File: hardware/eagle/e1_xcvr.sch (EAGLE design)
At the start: 48 parts, among them T1 BC847C

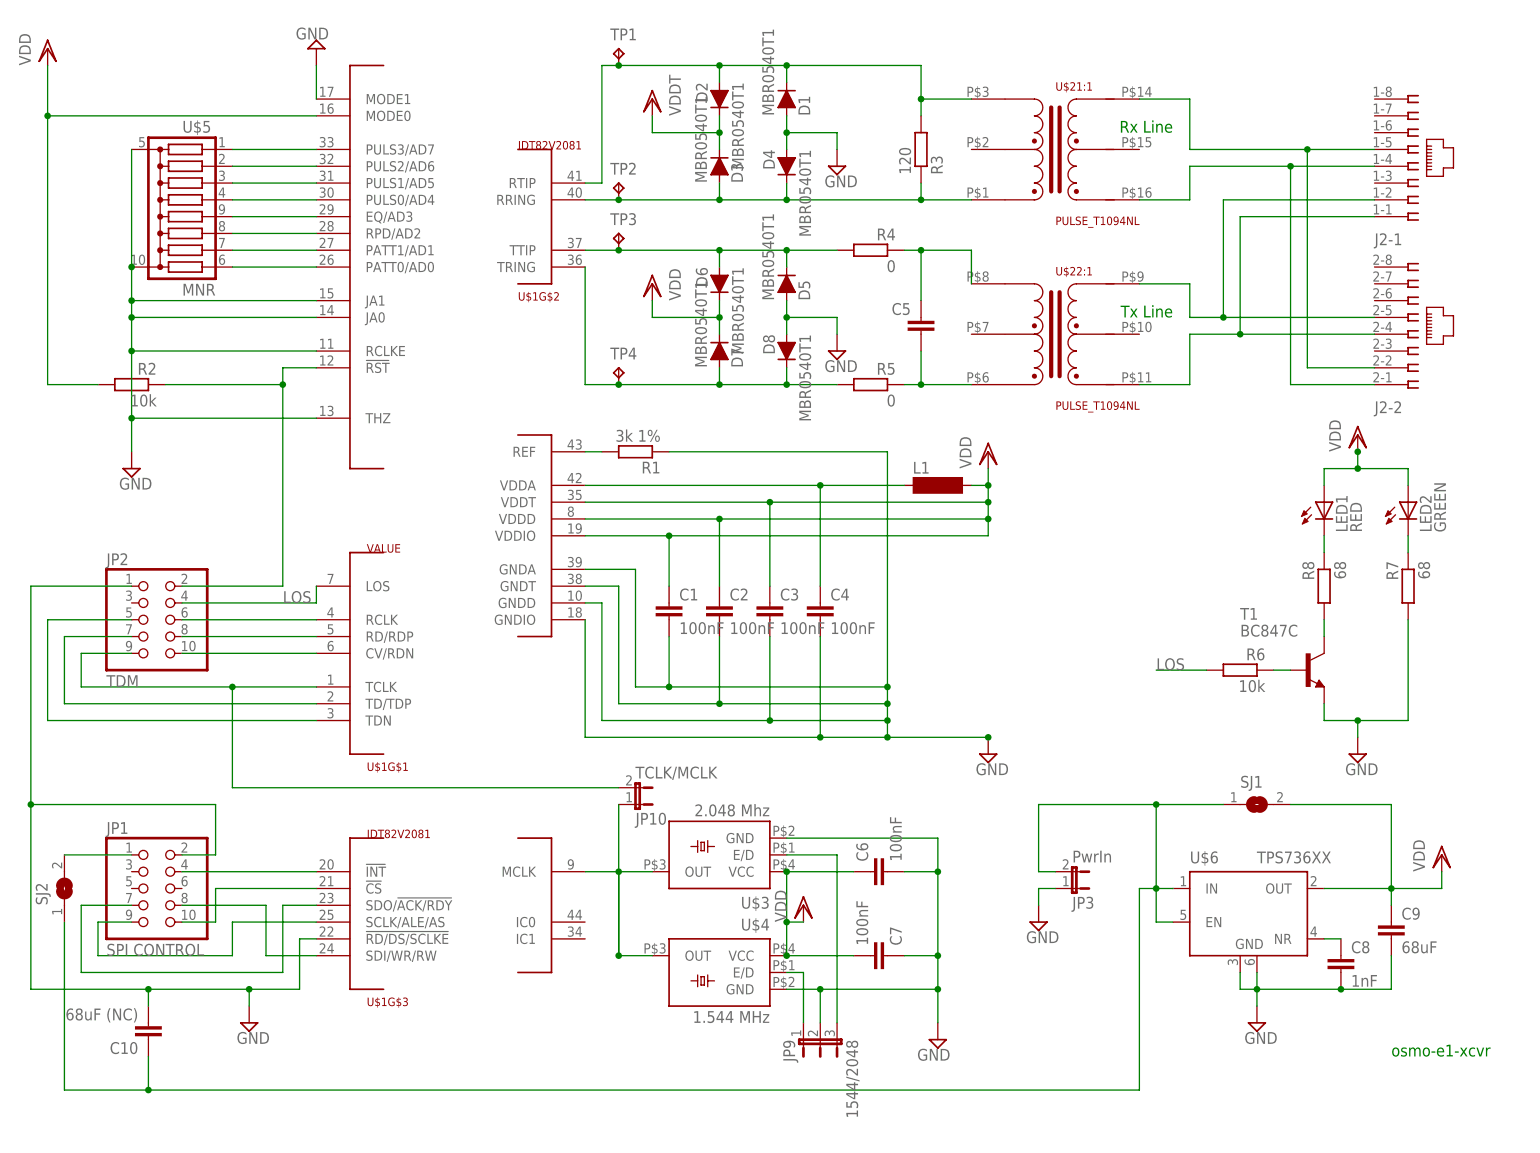
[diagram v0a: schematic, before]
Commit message: give parts names without "$", use 47nH as L1 (1206)
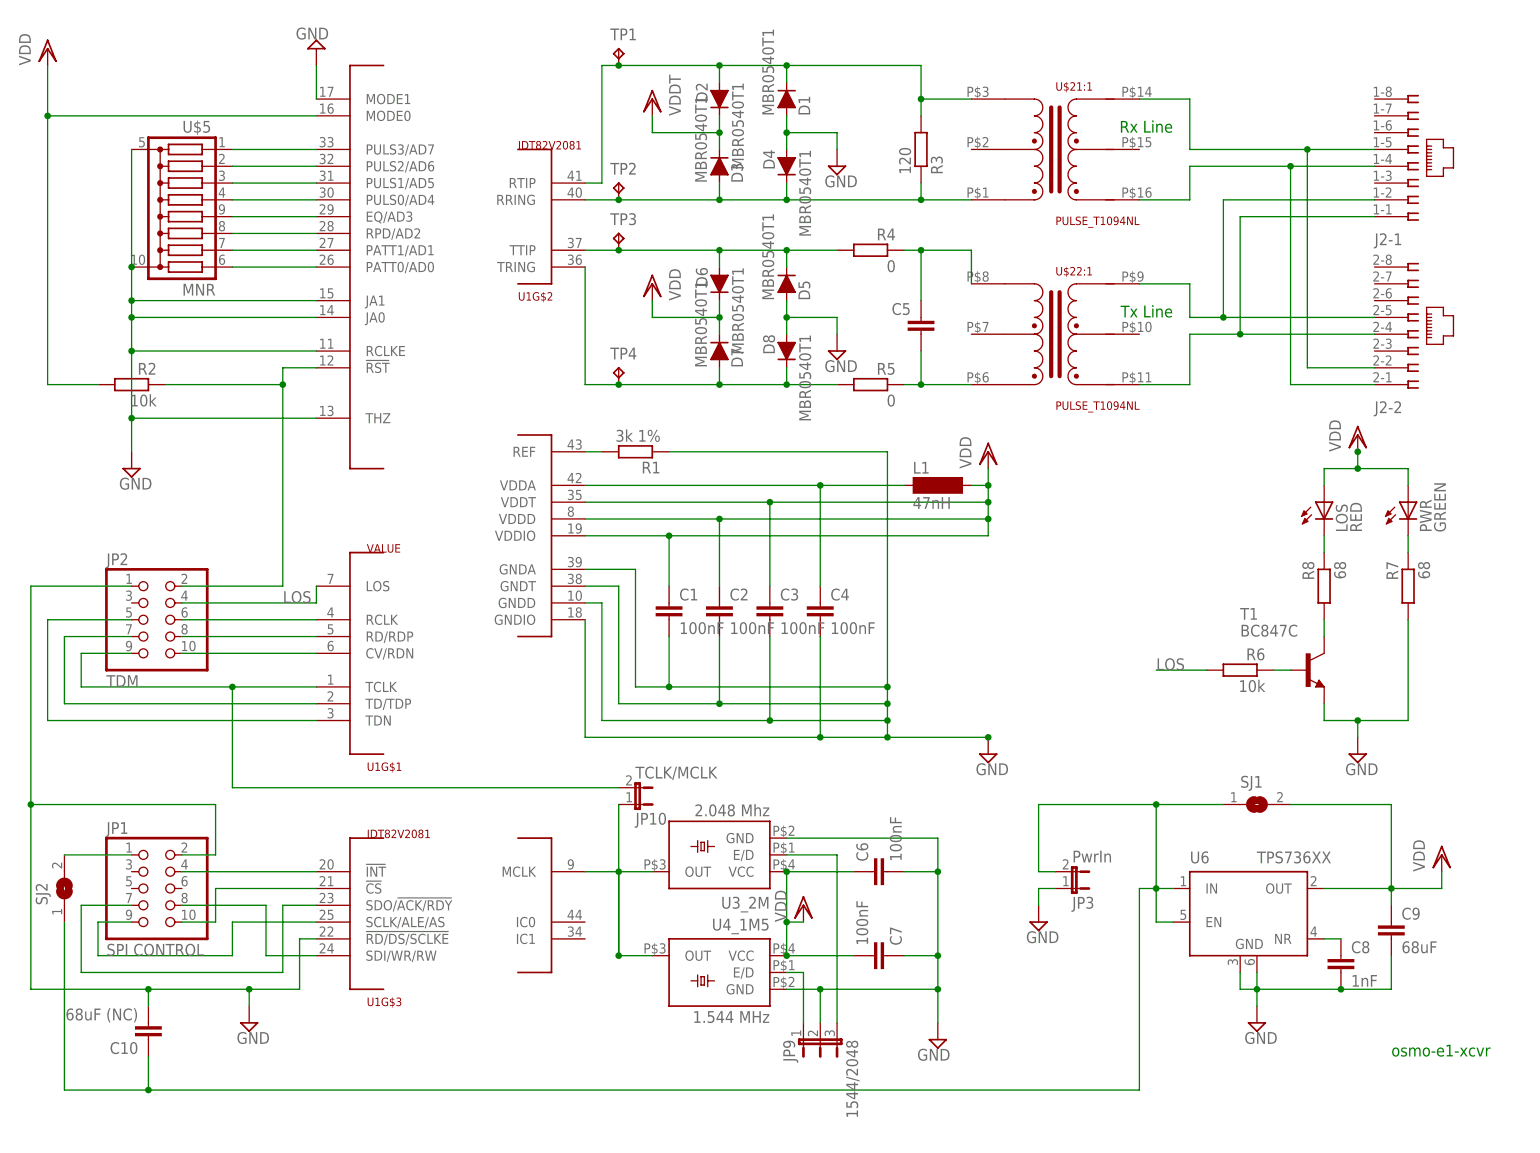
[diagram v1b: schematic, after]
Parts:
- L1: value (none) -> 47nH
- renumbered LED1 to LOS, LED2 to PWR, U$1 to U1, U$3 to U3_2M, U$4 to U4_1M5, U$6 to U6

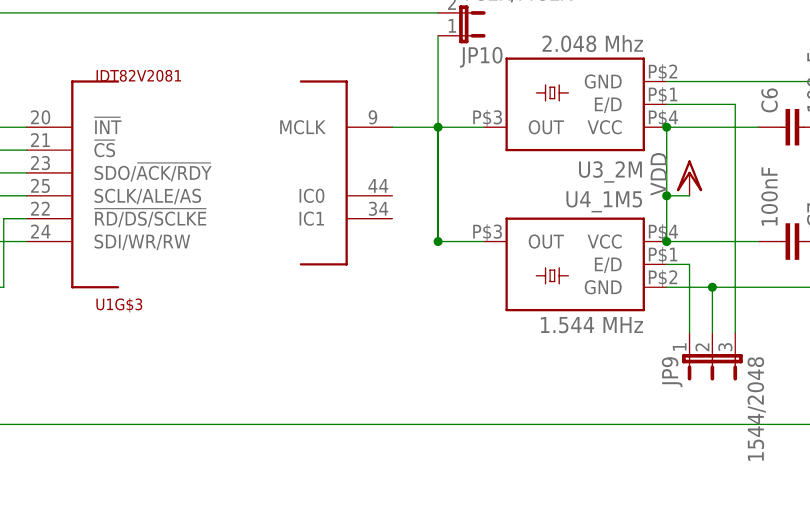
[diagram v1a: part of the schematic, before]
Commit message: connect LIU's pin 44 to GND (solves OSM#3247)
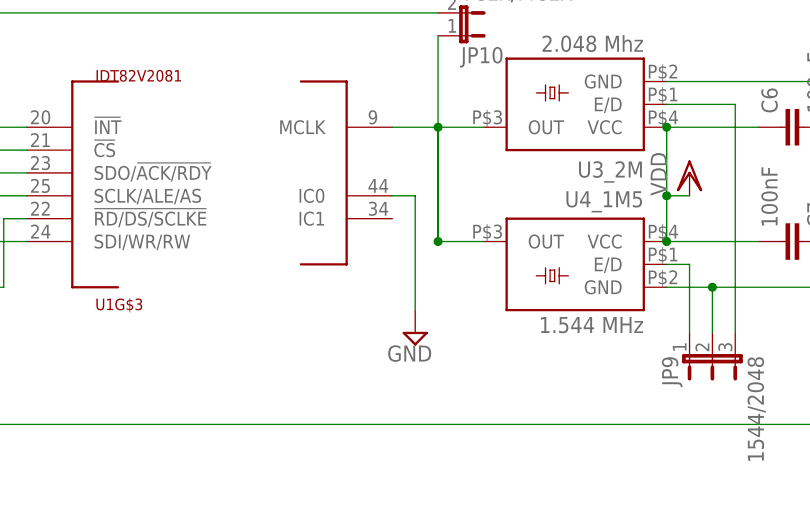
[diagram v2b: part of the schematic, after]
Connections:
- net GND: now also U1G$6.IC0
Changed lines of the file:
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@@
 <?xml version="1.0" encoding="utf-8"?>
 <!DOCTYPE eagle SYSTEM "eagle.dtd">
-<eagle version="6.0">
+<eagle version="7.6.0">
 <drawing>
 <settings>
@@
 <grid distance="0.1" unitdist="inch" unit="inch" style="lines" multiple="1" display="no" altdistance="0.01" altunitdist="inch" altunit="inch"/>
 <layers>
-<layer number="1" name="Top" color="4" fill="1" visible="no" active="no"/>
-<layer number="16" name="Bottom" color="1" fill="1" visible="no" active="no"/>
-<layer number="17" name="Pads" color="2" fill="1" visible="no" active="no"/>
-<layer number="18" name="Vias" color="2" fill="1" visible="no" active="no"/>
-<layer number="19" name="Unrouted" color="6" fill="1" visible="no" active="no"/>
-<layer number="20" name="Dimension" color="15" fill="1" visible="no" active="no"/>
-<layer number="21" name="tPlace" color="7" fill="1" visible="no" active="no"/>
-<layer number="22" name="bPlace" color="7" fill="1" visible="no" active="no"/>
-<layer number="23" name="tOrigins" color="15" fill="1" visible="no" active="no"/>
-<layer number="24" name="bOrigins" color="15" fill="1" visible="no" active="no"/>
-<layer number="25" name="tNames" color="7" fill="1" visible="no" active="no"/>
-<layer number="26" name="bNames" color="7" fill="1" visible="no" active="no"/>
-<layer number="27" name="tValues" color="7" fill="1" visible="no" active="no"/>
-<layer number="28" name="bValues" color="7" fill="1" visible="no" active="no"/>
+<layer number="1" name="Top" color="4" fill="1" visible="yes" active="no"/>
+<layer number="16" name="Bottom" color="1" fill="1" visible="yes" active="no"/>
+<layer number="17" name="Pads" color="2" fill="1" visible="yes" active="no"/>
+<layer number="18" name="Vias" color="2" fill="1" visible="yes" active="no"/>
+<layer number="19" name="Unrouted" color="6" fill="1" visible="yes" active="no"/>
+<layer number="20" name="Dimension" color="15" fill="1" visible="yes" active="no"/>
+<layer number="21" name="tPlace" color="7" fill="1" visible="yes" active="no"/>
+<layer number="22" name="bPlace" color="7" fill="1" visible="yes" active="no"/>
+<layer number="23" name="tOrigins" color="15" fill="1" visible="yes" active="no"/>
+<layer number="24" name="bOrigins" color="15" fill="1" visible="yes" active="no"/>
+<layer number="25" name="tNames" color="7" fill="1" visible="yes" active="no"/>
+<layer number="26" name="bNames" color="7" fill="1" visible="yes" active="no"/>
+<layer number="27" name="tValues" color="7" fill="1" visible="yes" active="no"/>
+<layer number="28" name="bValues" color="7" fill="1" visible="yes" active="no"/>
 <layer number="29" name="tStop" color="7" fill="3" visible="no" active="no"/>
 <layer number="30" name="bStop" color="7" fill="6" visible="no" active="no"/>
@@
 <layer number="35" name="tGlue" color="7" fill="4" visible="no" active="no"/>
 <layer number="36" name="bGlue" color="7" fill="5" visible="no" active="no"/>
-<layer number="37" name="tTest" color="7" fill="1" visible="no" active="no"/>
-<layer number="38" name="bTest" color="7" fill="1" visible="no" active="no"/>
+<layer number="37" name="tTest" color="7" fill="1" visible="yes" active="no"/>
+<layer number="38" name="bTest" color="7" fill="1" visible="yes" active="no"/>
 <layer number="39" name="tKeepout" color="4" fill="11" visible="no" active="no"/>
 <layer number="40" name="bKeepout" color="1" fill="11" visible="no" active="no"/>
@@
 <layer number="44" name="Drills" color="7" fill="1" visible="no" active="no"/>
 <layer number="45" name="Holes" color="7" fill="1" visible="no" active="no"/>
-<layer number="46" name="Milling" color="3" fill="1" visible="no" active="no"/>
-<layer number="47" name="Measures" color="7" fill="1" visible="no" active="no"/>
-<layer number="48" name="Document" color="7" fill="1" visible="no" active="no"/>
-<layer number="49" name="Reference" color="7" fill="1" visible="no" active="no"/>
-<layer number="51" name="tDocu" color="7" fill="1" visible="no" active="no"/>
-<layer number="52" name="bDocu" color="7" fill="1" visible="no" active="no"/>
+<layer number="46" name="Milling" color="3" fill="1" visible="yes" active="no"/>
+<layer number="47" name="Measures" color="7" fill="1" visible="yes" active="no"/>
+<layer number="48" name="Document" color="7" fill="1" visible="yes" active="no"/>
+<layer number="49" name="Reference" color="7" fill="1" visible="yes" active="no"/>
+<layer number="51" name="tDocu" color="7" fill="1" visible="yes" active="no"/>
+<layer number="52" name="bDocu" color="7" fill="1" visible="yes" active="no"/>
 <layer number="91" name="Nets" color="2" fill="1" visible="yes" active="yes"/>
 <layer number="92" name="Busses" color="1" fill="1" visible="yes" active="yes"/>
@@
 <part name="SUPPLY9" library="supply2" deviceset="GND" device=""/>
 <part name="SUPPLY10" library="supply2" deviceset="GND" device=""/>
+<part name="SUPPLY11" library="supply2" deviceset="GND" device=""/>
 </parts>
 <sheets>
@@
 <instance part="SUPPLY9" gate="GND" x="10.16" y="144.78"/>
 <instance part="SUPPLY10" gate="GND" x="27.94" y="60.96"/>
+<instance part="SUPPLY11" gate="GND" x="81.28" y="60.96" rot="MR0"/>
 </instances>
 <busses>
@@
 <pinref part="SUPPLY9" gate="GND" pin="GND"/>
 </segment>
+<segment>
+<pinref part="U1" gate="G$6" pin="IC0"/>
+<pinref part="SUPPLY11" gate="GND" pin="GND"/>
+<wire x1="78.74" y1="76.2" x2="81.28" y2="76.2" width="0.1524" layer="91"/>
+<wire x1="81.28" y1="76.2" x2="81.28" y2="63.5" width="0.1524" layer="91"/>
+</segment>
 </net>

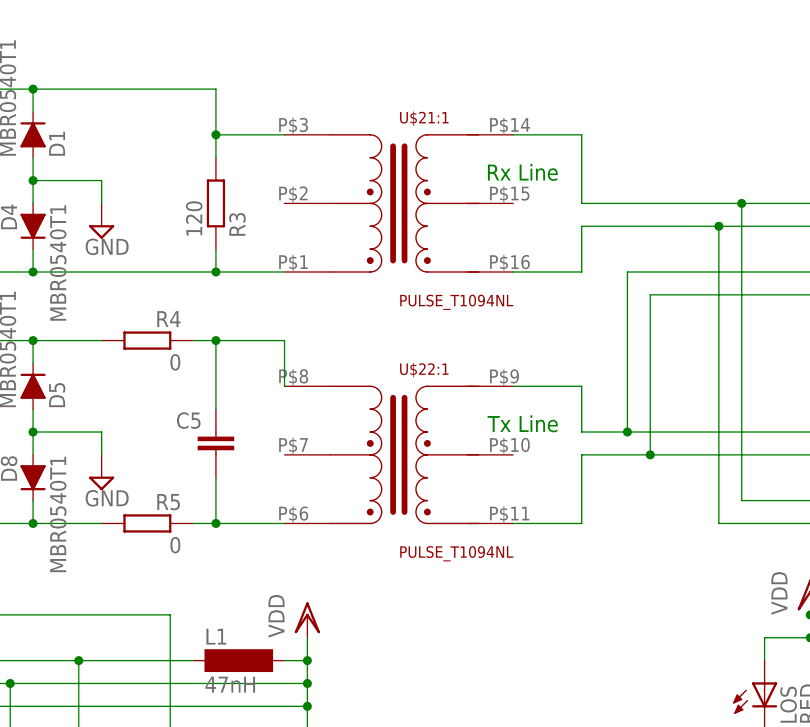
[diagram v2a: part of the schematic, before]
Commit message: replace old PULSE_T1094NL footprint, repair pin assignment (solves OSM#3269)
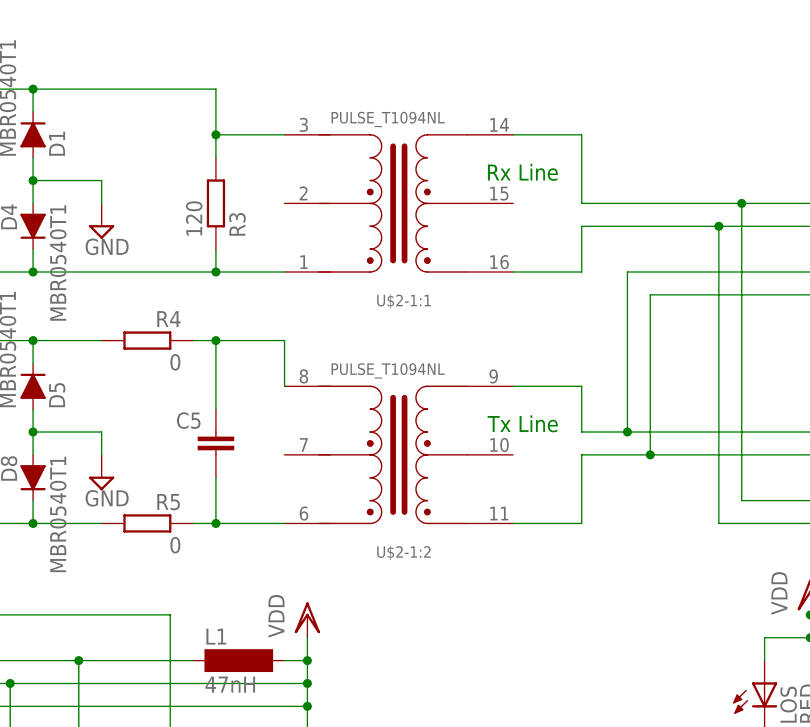
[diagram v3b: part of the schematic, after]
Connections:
- net N$29: now also U$2-1:2.P$6; no longer U$22:1.P$3
- net N$31: now also U$2-1:2.P$4; no longer U$22:1.P$1
- net N$32: now also U$2-1:2.P$3; no longer U$22:1.P$6
- net N$34: now also U$2-1:1.P$1; no longer U$21:1.P$4
- net N$36: now also U$2-1:2.P$1; no longer U$22:1.P$4
- net N$40: now also U$2-1:1.P$3; no longer U$21:1.P$6
- net RRING: now also U$2-1:1.P$4; no longer U$21:1.P$1
- net RTIP: now also U$2-1:1.P$6; no longer U$21:1.P$3
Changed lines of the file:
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@@
 <layers>
 <layer number="1" name="Top" color="4" fill="1" visible="yes" active="no"/>
+<layer number="2" name="Route2" color="1" fill="3" visible="yes" active="no"/>
+<layer number="3" name="Route3" color="4" fill="3" visible="yes" active="no"/>
+<layer number="14" name="Route14" color="1" fill="6" visible="yes" active="no"/>
+<layer number="15" name="Route15" color="4" fill="6" visible="yes" active="no"/>
 <layer number="16" name="Bottom" color="1" fill="1" visible="yes" active="no"/>
 <layer number="17" name="Pads" color="2" fill="1" visible="yes" active="no"/>
@@
 <instance part="C3" gate="G$1" x="106.68" y="124.46"/>
 <instance part="C4" gate="G$1" x="114.3" y="124.46"/>
-<instance part="U$2" gate="1:1" x="149.86" y="193.04" rot="MR180"/>
-<instance part="U$2" gate="2:1" x="149.86" y="165.1" rot="MR180"/>
+<instance part="U$2" gate="-1:1" x="149.86" y="193.04" rot="MR180"/>
+<instance part="U$2" gate="-1:2" x="149.86" y="165.1" rot="MR180"/>
 <instance part="R3" gate="G$1" x="129.54" y="193.04" rot="MR90"/>
 <instance part="D1" gate="G$1" x="109.22" y="200.66" rot="MR90"/>
@@
 <net name="RTIP" class="0">
 <segment>
-<pinref part="U$2" gate="1:1" pin="P$3"/>
+<pinref part="U$2" gate="-1:1" pin="P$6"/>
 <wire x1="137.16" y1="200.66" x2="129.54" y2="200.66" width="0.1524" layer="91"/>
 <pinref part="R3" gate="G$1" pin="2"/>
@@
 <net name="RRING" class="0">
 <segment>
-<pinref part="U$2" gate="1:1" pin="P$1"/>
+<pinref part="U$2" gate="-1:1" pin="P$4"/>
 <wire x1="137.16" y1="185.42" x2="129.54" y2="185.42" width="0.1524" layer="91"/>
 <pinref part="R3" gate="G$1" pin="1"/>
@@
 <net name="N$29" class="0">
 <segment>
-<pinref part="U$2" gate="2:1" pin="P$3"/>
+<pinref part="U$2" gate="-1:2" pin="P$6"/>
 <wire x1="137.16" y1="177.8" x2="137.16" y2="172.72" width="0.1524" layer="91"/>
 <pinref part="R4" gate="G$1" pin="1"/>
@@
 <segment>
 <pinref part="R5" gate="G$1" pin="1"/>
-<pinref part="U$2" gate="2:1" pin="P$1"/>
+<pinref part="U$2" gate="-1:2" pin="P$4"/>
 <wire x1="127" y1="157.48" x2="129.54" y2="157.48" width="0.1524" layer="91"/>
 <pinref part="C5" gate="G$1" pin="2"/>
@@
 <segment>
 <wire x1="170.18" y1="200.66" x2="162.56" y2="200.66" width="0.1524" layer="91"/>
-<pinref part="U$2" gate="1:1" pin="P$6"/>
+<pinref part="U$2" gate="-1:1" pin="P$3"/>
 <wire x1="170.18" y1="200.66" x2="170.18" y2="193.04" width="0.1524" layer="91"/>
 <pinref part="J2" gate="-1" pin="5"/>
@@
 <pinref part="J2" gate="-2" pin="1"/>
 <wire x1="185.42" y1="157.48" x2="198.12" y2="157.48" width="0.1524" layer="91"/>
-<pinref part="U$2" gate="1:1" pin="P$4"/>
+<pinref part="U$2" gate="-1:1" pin="P$1"/>
 <wire x1="170.18" y1="185.42" x2="162.56" y2="185.42" width="0.1524" layer="91"/>
 <wire x1="170.18" y1="185.42" x2="170.18" y2="190.5" width="0.1524" layer="91"/>
@@
 <pinref part="J2" gate="-1" pin="2"/>
 <wire x1="175.26" y1="185.42" x2="198.12" y2="185.42" width="0.1524" layer="91"/>
-<pinref part="U$2" gate="2:1" pin="P$6"/>
+<pinref part="U$2" gate="-1:2" pin="P$3"/>
 <wire x1="170.18" y1="172.72" x2="162.56" y2="172.72" width="0.1524" layer="91"/>
 <wire x1="170.18" y1="172.72" x2="170.18" y2="167.64" width="0.1524" layer="91"/>
@@
 <pinref part="J2" gate="-1" pin="1"/>
 <wire x1="177.8" y1="182.88" x2="198.12" y2="182.88" width="0.1524" layer="91"/>
-<pinref part="U$2" gate="2:1" pin="P$4"/>
+<pinref part="U$2" gate="-1:2" pin="P$1"/>
 <wire x1="170.18" y1="157.48" x2="162.56" y2="157.48" width="0.1524" layer="91"/>
 <wire x1="170.18" y1="157.48" x2="170.18" y2="165.1" width="0.1524" layer="91"/>
